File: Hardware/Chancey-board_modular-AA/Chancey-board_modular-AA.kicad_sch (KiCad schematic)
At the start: 114 parts, among them J1 QWIIC, U1 Hall_Sensor, U10 Hall_Sensor, U11 Hall_Sensor, U12 Hall_Sensor, U13 Hall_Sensor, U14 Hall_Sensor, U15 Hall_Sensor, U16 Hall_Sensor, U17 Hall_Sensor, U18 Hall_Sensor, U19 Hall_Sensor, U20 Hall_Sensor, U21 Hall_Sensor, U22 Hall_Sensor, U23 Hall_Sensor, U24 Hall_Sensor, U25 Hall_Sensor, U26 Hall_Sensor, U27 Hall_Sensor, U28 Hall_Sensor, U29 Hall_Sensor, U30 Hall_Sensor, U31 Hall_Sensor, U32 Hall_Sensor, U33 Hall_Sensor, U34 Hall_Sensor, U35 Hall_Sensor, U36 Hall_Sensor, U37 Hall_Sensor, U38 Hall_Sensor, U39 Hall_Sensor, U40 Hall_Sensor, U41 Hall_Sensor, U42 Hall_Sensor, U43 Hall_Sensor, U44 Hall_Sensor, U45 Hall_Sensor, U46 Hall_Sensor, U47 Hall_Sensor, U48 Hall_Sensor, U49 Hall_Sensor, U50 Hall_Sensor, U51 Hall_Sensor, U52 Hall_Sensor, U53 Hall_Sensor, U54 Hall_Sensor, U55 Hall_Sensor, U56 Hall_Sensor, U57 Hall_Sensor, U58 Hall_Sensor, U59 Hall_Sensor, U6 BlackPill_STLINK, U60 Hall_Sensor, U61 Hall_Sensor, U62 Hall_Sensor, U63 Hall_Sensor, U64 Hall_Sensor, U65 Hall_Sensor, U66 Hall_Sensor, U67 Hall_Sensor, U68 Hall_Sensor, U69 Hall_Sensor, U7 Hall_Sensor, U70 Hall_Sensor, U71 Hall_Sensor, U72 Hall_Sensor, U73 Hall_Sensor, U74 Hall_Sensor, U75 Hall_Sensor, U76 Hall_Sensor, U8 Hall_Sensor, U9 Hall_Sensor

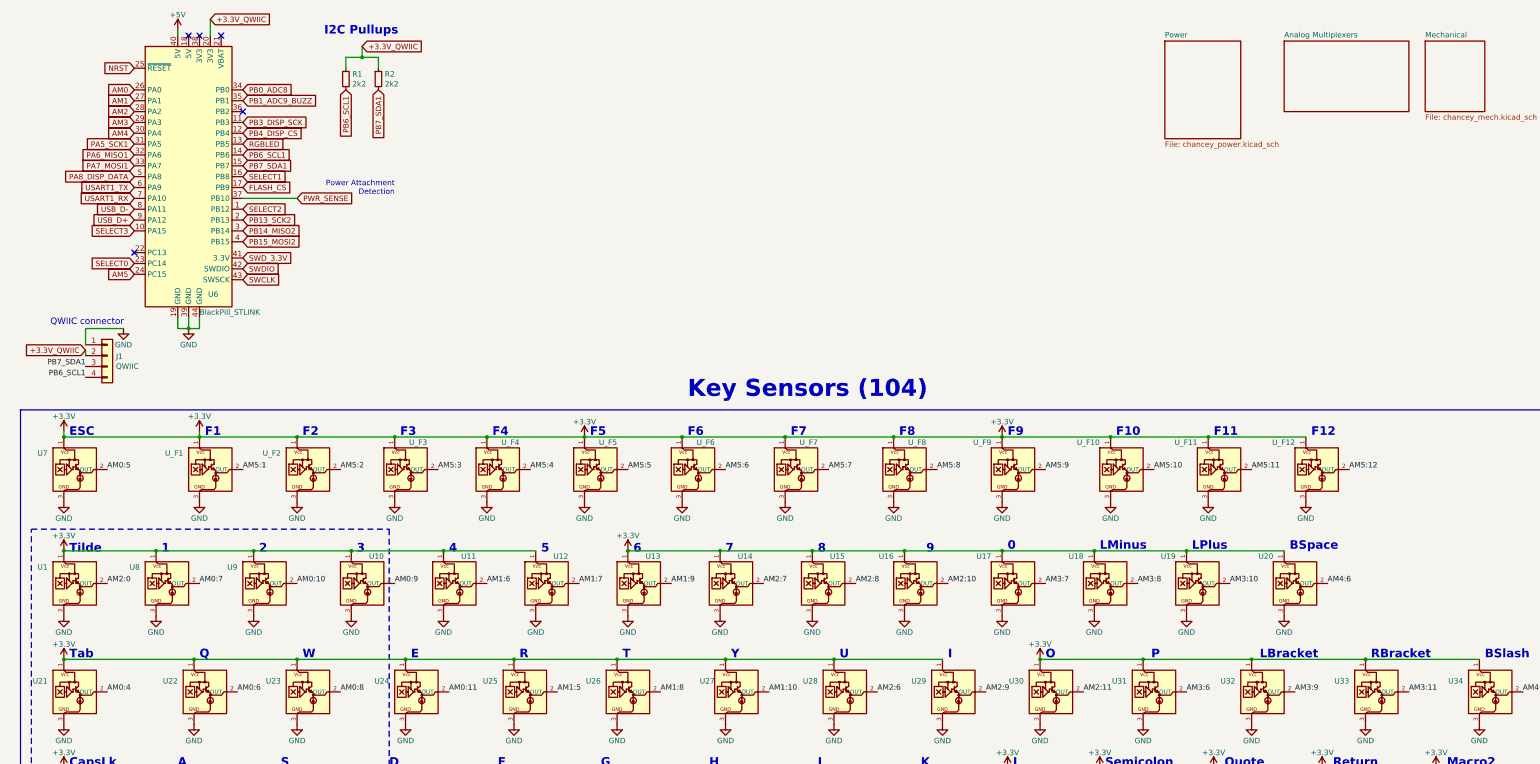
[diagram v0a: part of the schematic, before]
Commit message: Changed many global labels to hierarchical and local labels.
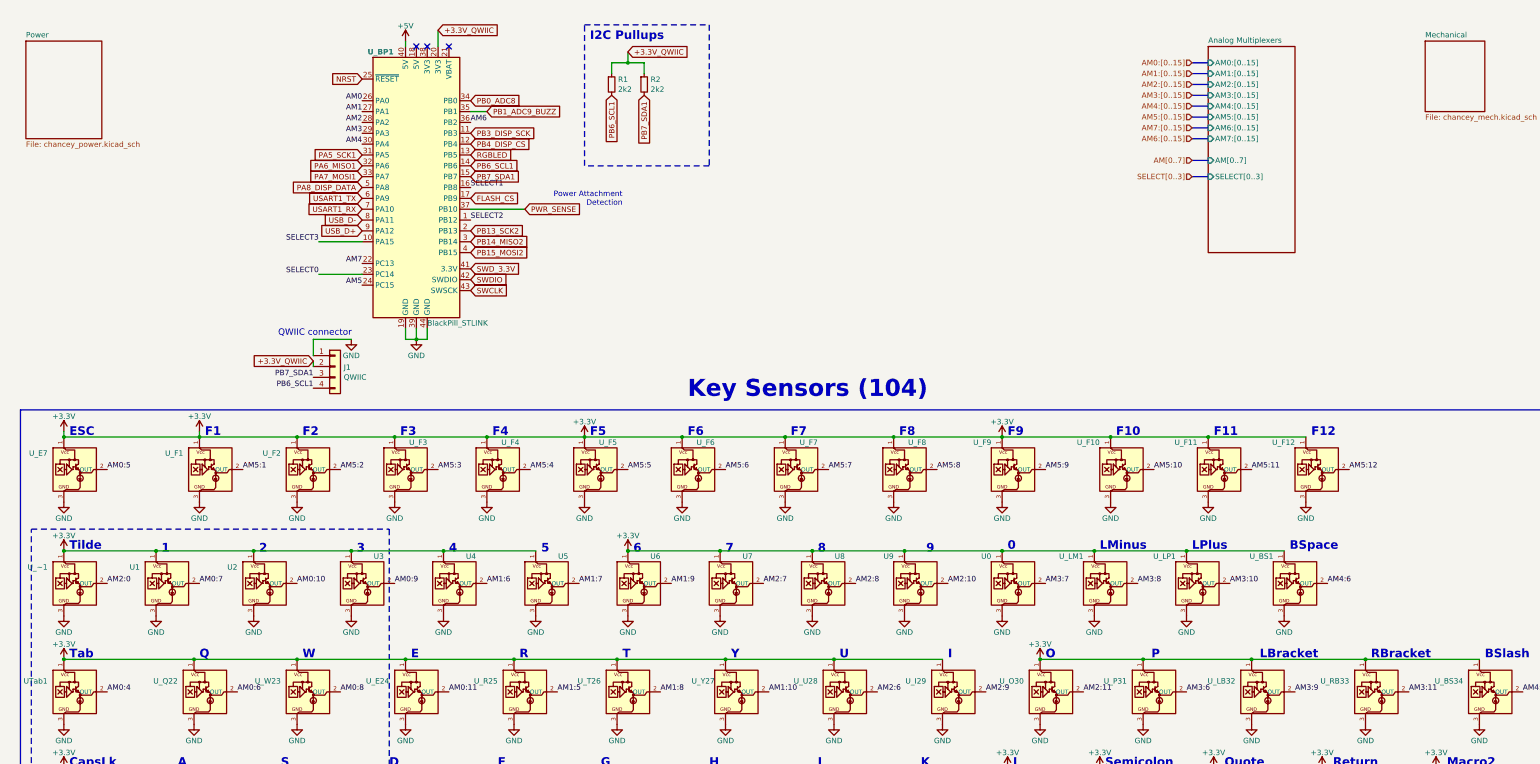
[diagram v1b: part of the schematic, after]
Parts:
- U_BP1: renamed from U6; footprint blackpill:BlackPill_STLINK -> Chancey_modular:BlackPill_STLINK
- renumbered U17 to U0, U8 to U1, U9 to U2, U10 to U3, U11 to U4, U12 to U5, U13 to U6, U14 to U7, U15 to U8, U16 to U9, U21 to UTab1, U20 to U_BS1, U34 to U_BS34, U24 to U_E24, U7 to U_E7, U29 to U_I29, U32 to U_LB32, U18 to U_LM1, U19 to U_LP1, U30 to U_O30, U31 to U_P31, U22 to U_Q22, U25 to U_R25, U33 to U_RB33, U26 to U_T26, U28 to U_U28, U23 to U_W23, U27 to U_Y27, U1 to U_~1
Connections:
- net AM7: now reaches U_BP1.22 (PC13)
- net AM6: now reaches U_BP1.36 (PB2)
- no-connect marks 5 -> 3
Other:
- sheet Analog Multiplexers ports: added AM0:[0..15], AM1:[0..15], AM2:[0..15], AM3:[0..15], AM4:[0..15], AM5:[0..15], AM6:[0..15], AM7:[0..15], AM[0..7], SELECT[0..3]; removed none
- moved on the sheet: J1, R1, R2, U_BP1
